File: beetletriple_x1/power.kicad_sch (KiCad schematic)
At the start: 24 parts, among them U1 TPS54331DR, U2 HT7550-1, U4 78L12G-AB3-R

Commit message: Footprints shenanigans
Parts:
- added C?: 10uF 50V, Capacitor_SMD:C_1206_3216Metric, symbol Device:C
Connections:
- net +12V: now also C?.1
- net GND: now also C?.2
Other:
- moved on the sheet: C14
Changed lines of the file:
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@@
   (junction (at 51.435 38.735) (diameter 1.016) (color 0 0 0 0))
   (junction (at 57.15 66.675) (diameter 1.016) (color 0 0 0 0))
-  (junction (at 62.865 104.14) (diameter 0.9144) (color 0 0 0 0))
+  (junction (at 58.42 104.14) (diameter 0.9144) (color 0 0 0 0))
+  (junction (at 58.42 115.57) (diameter 0.9144) (color 0 0 0 0))
   (junction (at 69.85 191.135) (diameter 0.9144) (color 0 0 0 0))
   (junction (at 70.485 38.735) (diameter 1.016) (color 0 0 0 0))
   (junction (at 70.485 46.355) (diameter 1.016) (color 0 0 0 0))
+  (junction (at 71.755 104.14) (diameter 0.9144) (color 0 0 0 0))
   (junction (at 74.295 46.355) (diameter 0.9144) (color 0 0 0 0))
   (junction (at 76.2 38.735) (diameter 0.9144) (color 0 0 0 0))
@@
     (stroke (width 0) (type solid) (color 0 0 0 0))
   )
-  (wire (pts (xy 56.515 104.14) (xy 62.865 104.14))
+  (wire (pts (xy 56.515 104.14) (xy 58.42 104.14))
     (stroke (width 0) (type solid) (color 0 0 0 0))
   )
@@
     (stroke (width 0) (type solid) (color 0 0 0 0))
   )
+  (wire (pts (xy 58.42 104.14) (xy 71.755 104.14))
+    (stroke (width 0) (type solid) (color 0 0 0 0))
+  )
+  (wire (pts (xy 58.42 111.76) (xy 58.42 115.57))
+    (stroke (width 0) (type solid) (color 0 0 0 0))
+  )
+  (wire (pts (xy 58.42 115.57) (xy 48.895 115.57))
+    (stroke (width 0) (type solid) (color 0 0 0 0))
+  )
+  (wire (pts (xy 58.42 115.57) (xy 71.755 115.57))
+    (stroke (width 0) (type solid) (color 0 0 0 0))
+  )
   (wire (pts (xy 62.23 173.355) (xy 62.23 173.99))
     (stroke (width 0) (type solid) (color 0 0 0 0))
   )
-  (wire (pts (xy 62.865 104.14) (xy 76.835 104.14))
-    (stroke (width 0) (type solid) (color 0 0 0 0))
-  )
-  (wire (pts (xy 62.865 111.76) (xy 62.865 115.57))
-    (stroke (width 0) (type solid) (color 0 0 0 0))
-  )
-  (wire (pts (xy 62.865 115.57) (xy 48.895 115.57))
-    (stroke (width 0) (type solid) (color 0 0 0 0))
-  )
   (wire (pts (xy 69.85 181.61) (xy 69.85 191.135))
     (stroke (width 0) (type solid) (color 0 0 0 0))
@@
   )
   (wire (pts (xy 70.485 38.735) (xy 76.2 38.735))
+    (stroke (width 0) (type solid) (color 0 0 0 0))
+  )
+  (wire (pts (xy 71.755 104.14) (xy 76.835 104.14))
+    (stroke (width 0) (type solid) (color 0 0 0 0))
+  )
+  (wire (pts (xy 71.755 115.57) (xy 71.755 111.76))
     (stroke (width 0) (type solid) (color 0 0 0 0))
   )
@@
     (pin "2")
   )
-  (symbol (lib_id "Device:C") (at 62.865 107.95 0) (unit 1)
-    (in_bom yes) (on_board yes)
-    (property "Reference" "C14" (id 0) (at 65.786 106.801 0)
-      (effects (font (size 1.27 1.27)) (justify left))
-    )
-    (property "Value" "2.2uF 50V" (id 1) (at 65.7861 109.0993 0)
-      (effects (font (size 1.27 1.27)) (justify left))
-    )
-    (property "Footprint" "Capacitor_SMD:C_1206_3216Metric" (id 2) (at 63.8302 111.76 0)
-      (effects (font (size 1.27 1.27)) hide)
-    )
-    (property "Datasheet" "~" (id 3) (at 62.865 107.95 0)
-      (effects (font (size 1.27 1.27)) hide)
-    )
-    (property "LCSC" "C50254" (id 4) (at 62.865 107.95 0)
+  (symbol (lib_id "Device:C") (at 58.42 107.95 0) (unit 1)
+    (in_bom yes) (on_board yes)
+    (property "Reference" "C?" (id 0) (at 61.3411 106.8006 0)
+      (effects (font (size 1.27 1.27)) (justify left))
+    )
+    (property "Value" "10uF 50V" (id 1) (at 61.3411 109.0993 0)
+      (effects (font (size 1.27 1.27)) (justify left))
+    )
+    (property "Footprint" "Capacitor_SMD:C_1206_3216Metric" (id 2) (at 59.3852 111.76 0)
+      (effects (font (size 1.27 1.27)) hide)
+    )
+    (property "Datasheet" "~" (id 3) (at 58.42 107.95 0)
+      (effects (font (size 1.27 1.27)) hide)
+    )
+    (property "LCSC" "C13585" (id 4) (at 58.42 107.95 0)
       (effects (font (size 1.27 1.27)) hide)
     )
@@
       (effects (font (size 1.27 1.27)) hide)
     )
+    (pin "1")
+    (pin "2")
+  )
+  (symbol (lib_id "Device:C") (at 71.755 107.95 0) (unit 1)
+    (in_bom yes) (on_board yes)
+    (property "Reference" "C14" (id 0) (at 74.676 106.801 0)
+      (effects (font (size 1.27 1.27)) (justify left))
+    )
+    (property "Value" "2.2uF 50V" (id 1) (at 74.6761 109.0993 0)
+      (effects (font (size 1.27 1.27)) (justify left))
+    )
+    (property "Footprint" "Capacitor_SMD:C_1206_3216Metric" (id 2) (at 72.7202 111.76 0)
+      (effects (font (size 1.27 1.27)) hide)
+    )
+    (property "Datasheet" "~" (id 3) (at 71.755 107.95 0)
+      (effects (font (size 1.27 1.27)) hide)
+    )
+    (property "LCSC" "C50254" (id 4) (at 71.755 107.95 0)
+      (effects (font (size 1.27 1.27)) hide)
+    )

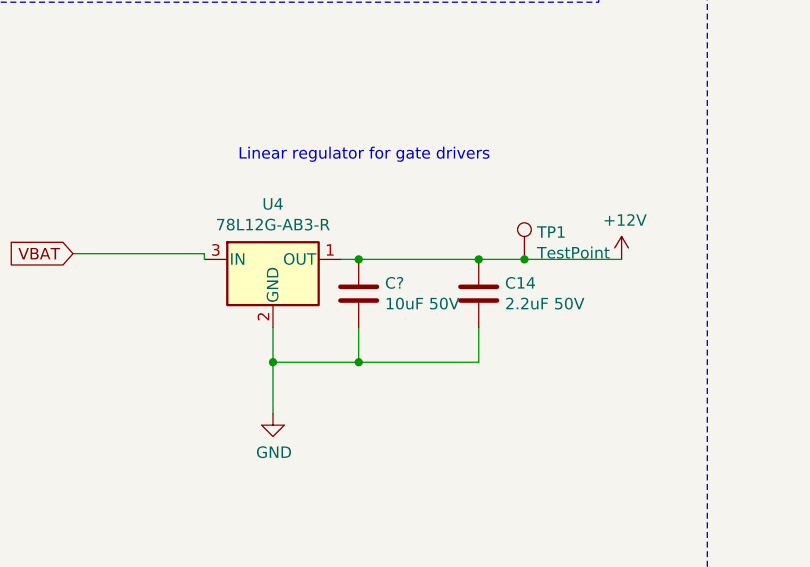
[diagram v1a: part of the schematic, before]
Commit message: Add another capacitor on 12v line
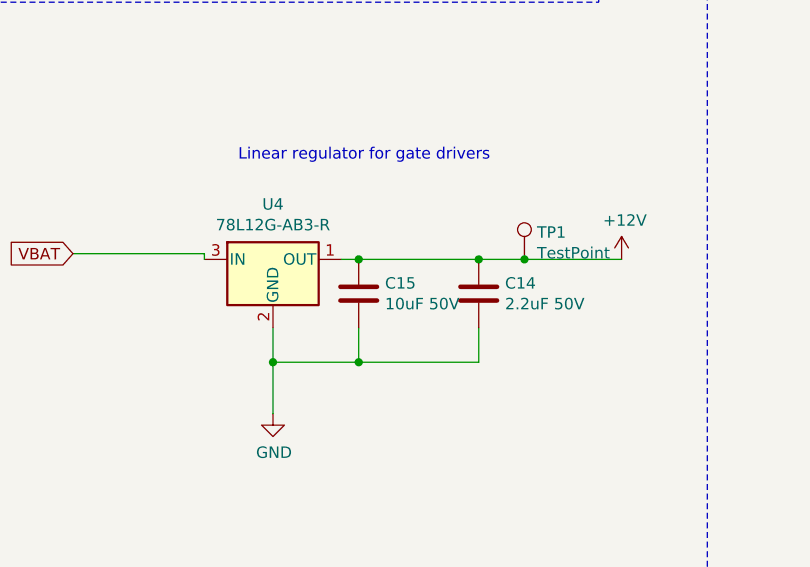
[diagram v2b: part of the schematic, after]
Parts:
- gave numbers to parts that had none: 1
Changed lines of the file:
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@@
   (symbol (lib_id "Device:C") (at 58.42 107.95 0) (unit 1)
     (in_bom yes) (on_board yes)
-    (property "Reference" "C?" (id 0) (at 61.3411 106.8006 0)
+    (property "Reference" "C15" (id 0) (at 61.3411 106.8006 0)
       (effects (font (size 1.27 1.27)) (justify left))
     )

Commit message: minor updates
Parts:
- F1: footprint beetletriple:fuseholder_flexible -> beetletriple:fuseholder_bs1363
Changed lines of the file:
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@@
     (property "Reference" "F1" (id 0) (at 36.83 33.7628 90))
     (property "Value" "20mmx5 fuse holder" (id 1) (at 36.83 36.061 90))
-    (property "Footprint" "beetletriple:fuseholder_flexible" (id 2) (at 36.83 40.513 90)
+    (property "Footprint" "beetletriple:fuseholder_bs1363" (id 2) (at 36.83 40.513 90)
       (effects (font (size 1.27 1.27)) hide)
     )
